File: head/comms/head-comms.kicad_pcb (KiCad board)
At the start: 2 copper layers, 30 x 20 mm, 40 parts, among them J1 conn_head_main, J3 USB_C_Receptacle_USB2.0_16P, J4 conn_chest, U1 LM66200, U2 SP48xE, U3 USBLC6-2SC6, U4 RP509x, U5 RTL8189FTV-VC-CG, Y3 26M

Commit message: finishing touches
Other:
- board text added: "GRG4UQ"
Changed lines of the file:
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@@
 		(rev "1")
 		(company "team noon")
-		(comment 1 "NanoID: rI02tsXA")
+		(comment 1 "NanoID: GRG4UQ")
 		(comment 3 "github.com/team-noon/hw1")
 		(comment 4 "Drawn By: Sam")
@@
 			(outputformat 1)
 			(mirror no)
-			(drillshape 1)
+			(drillshape 0)
 			(scaleselection 1)
-			(outputdirectory "")
+			(outputdirectory "export/")
 		)
 	)
@@
 		(layer "Edge.Cuts")
 	)
+	(gr_text "GRG4UQ"
+		(at 65 52.45 0)
+		(layer "F.SilkS")
+		(effects
+			(font
+				(size 1.5 1.5)
+				(thickness 0.3)
+				(bold yes)
+			)
+		)
+	)
 	(segment
 		(start 67.840001 66.872498)
@@
 	)
 	(segment
+		(start 71.990001 61.75)
+		(end 71.3 61.75)
+		(width 0.2)
+		(layer "F.Cu")
+		(net "Net-(J3-CC2)")
+	)
+	(via
+		(at 71.3 61.75)
+		(size 0.5)
+		(drill 0.3)
+		(layers "F.Cu" "B.Cu")
+		(net "Net-(J3-CC2)")
+	)
+	(segment
+		(start 71.3 61.75)
+		(end 72.305 61.75)
+		(width 0.2)
+		(layer "B.Cu")
+		(net "Net-(J3-CC2)")
+	)
+	(segment
 		(start 59.6 61.28)
 		(end 59.6 61.75)
@@
 	)
 	(segment
+		(start 71.99 58.75)
+		(end 71.3 58.75)
+		(width 0.2)
+		(layer "F.Cu")
+		(net "Net-(J3-CC1)")
+	)
+	(via
+		(at 71.3 58.75)
+		(size 0.5)
+		(drill 0.3)
+		(layers "F.Cu" "B.Cu")
+		(net "Net-(J3-CC1)")
+	)
+	(segment
+		(start 71.3 58.75)
+		(end 72.305 58.75)
+		(width 0.2)
+		(layer "B.Cu")
+		(net "Net-(J3-CC1)")
+	)
+	(segment
 		(start 58.5 57.485)
 		(end 58.5 58.5375)
@@
 	)
 	(segment
+		(start 72.305 60.75)
+		(end 70.924129 60.75)
+		(width 0.2)
+		(layer "B.Cu")
+		(net "Net-(J3-D+-PadA6)")
+	)
+	(segment
+		(start 70.924129 60.75)
+		(end 70.549129 61.125)
+		(width 0.2)
+		(layer "B.Cu")
+		(net "Net-(J3-D+-PadA6)")
+	)
+	(segment
+		(start 70.549129 61.125)
+		(end 69.00087 61.125)
+		(width 0.2)
+		(layer "B.Cu")
+		(net "Net-(J3-D+-PadA6)")
+	)
+	(segment
+		(start 73.05 60.75)
+		(end 72.305 60.75)
+		(width 0.2)
+		(layer "B.Cu")
+		(net "Net-(J3-D+-PadA6)")
+	)
+	(segment
+		(start 72.305 59.75)
+		(end 73.08 59.75)
+		(width 0.2)
+		(layer "B.Cu")
+		(net "Net-(J3-D+-PadA6)")
+	)
+	(segment
+		(start 68.350001 60.474131)
+		(end 68.350001 60.2625)
+		(width 0.2)
+		(layer "B.Cu")
+		(net "Net-(J3-D+-PadA6)")
+	)
+	(segment
+		(start 73.23 59.9)
+		(end 73.23 60.57)
+		(width 0.2)
+		(layer "B.Cu")
+		(net "Net-(J3-D+-PadA6)")
+	)
+	(segment
+		(start 69.00087 61.125)
+		(end 68.350001 60.474131)
+		(width 0.2)
+		(layer "B.Cu")
+		(net "Net-(J3-D+-PadA6)")
+	)
+	(segment
+		(start 73.23 60.57)
+		(end 73.05 60.75)
+		(width 0.2)
+		(layer "B.Cu")
+		(net "Net-(J3-D+-PadA6)")
+	)
+	(segment
+		(start 73.08 59.75)
+		(end 73.23 59.9)
+		(width 0.2)
+		(layer "B.Cu")
+		(net "Net-(J3-D+-PadA6)")
+	)
+	(segment
 		(start 69.3 60.2625)
 		(end 69.3 59.600001)
@@
 	)
 	(segment
+		(start 71.53 59.25)
+		(end 72.305 59.25)
+		(width 0.2)
+		(layer "B.Cu")
+		(net "Net-(J3-D--PadA7)")
+	)
+	(segment
+		(start 71.53 60.25)
+		(end 71.38 60.1)
+		(width 0.2)
+		(layer "B.Cu")
+		(net "Net-(J3-D--PadA7)")
+	)
+	(segment
+		(start 70.262499 60.25)
+		(end 70.249999 60.2625)
+		(width 0.2)
+		(layer "B.Cu")
+		(net "Net-(J3-D--PadA7)")
+	)
+	(segment
+		(start 72.305 60.25)
+		(end 71.53 60.25)
+		(width 0.2)
+		(layer "B.Cu")
+		(net "Net-(J3-D--PadA7)")
+	)
+	(segment
+		(start 71.38 60.1)
+		(end 71.38 59.4)
+		(width 0.2)
+		(layer "B.Cu")
+		(net "Net-(J3-D--PadA7)")
+	)
+	(segment
+		(start 72.305 60.25)
+		(end 70.262499 60.25)
+		(width 0.2)
+		(layer "B.Cu")
+		(net "Net-(J3-D--PadA7)")
+	)
+	(segment
+		(start 71.38 59.4)
+		(end 71.53 59.25)
+		(width 0.2)
+		(layer "B.Cu")
+		(net "Net-(J3-D--PadA7)")
+	)
+	(segment
 		(start 65.900001 63)
 		(end 65.8 63.100001)
@@
 		(net "/WiFi/XO")
 	)
-	(segment
-		(start 71.53 59.25)
-		(end 72.305 59.25)
-		(width 0.2)
-		(layer "B.Cu")
-		(net "Net-(J3-D--PadA7)")
-	)
-	(segment
-		(start 71.53 60.25)
-		(end 71.38 60.1)
-		(width 0.2)
-		(layer "B.Cu")
-		(net "Net-(J3-D--PadA7)")
-	)
-	(segment
-		(start 70.262499 60.25)
-		(end 70.249999 60.2625)
-		(width 0.2)
-		(layer "B.Cu")
-		(net "Net-(J3-D--PadA7)")
-	)
-	(segment
-		(start 72.305 60.25)
-		(end 71.53 60.25)
-		(width 0.2)
-		(layer "B.Cu")
-		(net "Net-(J3-D--PadA7)")
-	)
-	(segment
-		(start 71.38 60.1)
-		(end 71.38 59.4)
-		(width 0.2)
-		(layer "B.Cu")
-		(net "Net-(J3-D--PadA7)")
-	)
-	(segment
-		(start 72.305 60.25)
-		(end 70.262499 60.25)
-		(width 0.2)
-		(layer "B.Cu")
-		(net "Net-(J3-D--PadA7)")
-	)
-	(segment
-		(start 71.38 59.4)
-		(end 71.53 59.25)
-		(width 0.2)
-		(layer "B.Cu")
-		(net "Net-(J3-D--PadA7)")
-	)
-	(segment
-		(start 71.99 58.75)
-		(end 71.3 58.75)
-		(width 0.2)
-		(layer "F.Cu")
-		(net "Net-(J3-CC1)")
-	)
-	(via
-		(at 71.3 58.75)
-		(size 0.5)
-		(drill 0.3)
-		(layers "F.Cu" "B.Cu")
-		(net "Net-(J3-CC1)")
-	)
-	(segment
-		(start 71.3 58.75)
-		(end 72.305 58.75)
-		(width 0.2)
-		(layer "B.Cu")
-		(net "Net-(J3-CC1)")
-	)
-	(segment
-		(start 72.305 60.75)
-		(end 70.924129 60.75)
-		(width 0.2)
-		(layer "B.Cu")
-		(net "Net-(J3-D+-PadA6)")
-	)
-	(segment
-		(start 70.924129 60.75)
-		(end 70.549129 61.125)
-		(width 0.2)
-		(layer "B.Cu")
-		(net "Net-(J3-D+-PadA6)")
-	)
-	(segment
-		(start 70.549129 61.125)
-		(end 69.00087 61.125)
-		(width 0.2)
-		(layer "B.Cu")
-		(net "Net-(J3-D+-PadA6)")
-	)
-	(segment
-		(start 73.05 60.75)
-		(end 72.305 60.75)
-		(width 0.2)
-		(layer "B.Cu")
-		(net "Net-(J3-D+-PadA6)")
-	)
-	(segment
-		(start 72.305 59.75)
-		(end 73.08 59.75)
-		(width 0.2)
-		(layer "B.Cu")
-		(net "Net-(J3-D+-PadA6)")
-	)
-	(segment
-		(start 68.350001 60.474131)
-		(end 68.350001 60.2625)
-		(width 0.2)
-		(layer "B.Cu")
-		(net "Net-(J3-D+-PadA6)")
-	)
-	(segment
-		(start 73.23 59.9)
-		(end 73.23 60.57)
-		(width 0.2)
-		(layer "B.Cu")
-		(net "Net-(J3-D+-PadA6)")
-	)
-	(segment
-		(start 69.00087 61.125)
-		(end 68.350001 60.474131)
-		(width 0.2)
-		(layer "B.Cu")
-		(net "Net-(J3-D+-PadA6)")
-	)
-	(segment
-		(start 73.23 60.57)
-		(end 73.05 60.75)
-		(width 0.2)
-		(layer "B.Cu")
-		(net "Net-(J3-D+-PadA6)")
-	)
-	(segment
-		(start 73.08 59.75)
-		(end 73.23 59.9)
-		(width 0.2)
-		(layer "B.Cu")
-		(net "Net-(J3-D+-PadA6)")
-	)
-	(segment
-		(start 71.990001 61.75)
-		(end 71.3 61.75)
-		(width 0.2)
-		(layer "F.Cu")
-		(net "Net-(J3-CC2)")
-	)
-	(via
-		(at 71.3 61.75)
-		(size 0.5)
-		(drill 0.3)
-		(layers "F.Cu" "B.Cu")
-		(net "Net-(J3-CC2)")
-	)
-	(segment
-		(start 71.3 61.75)
-		(end 72.305 61.75)
-		(width 0.2)
-		(layer "B.Cu")
-		(net "Net-(J3-CC2)")
-	)
 	(zone

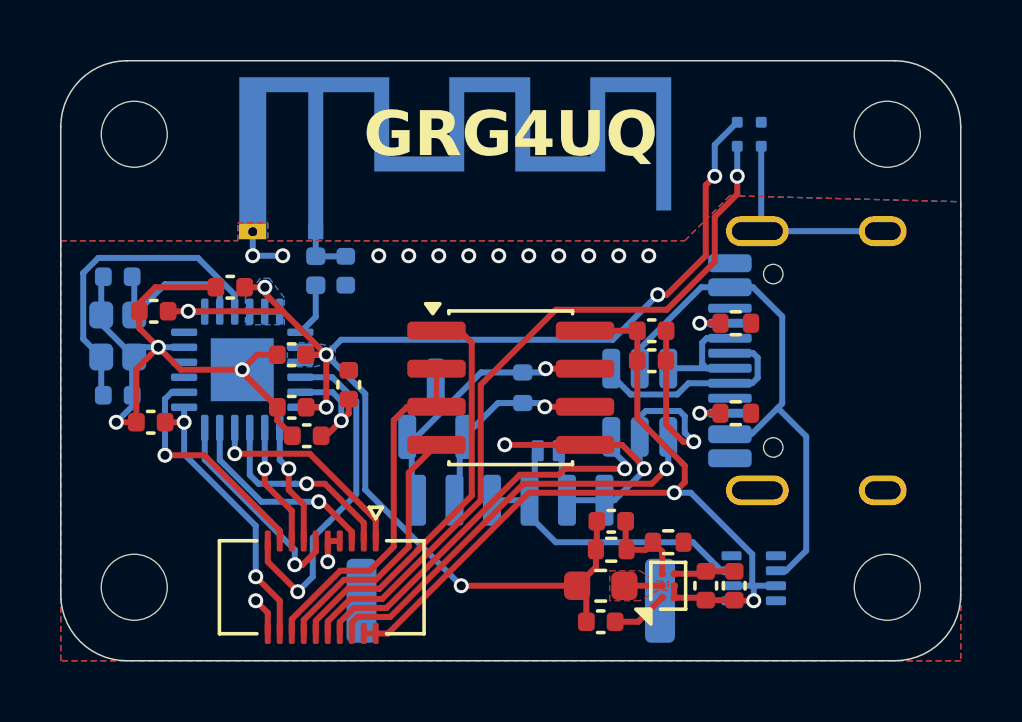
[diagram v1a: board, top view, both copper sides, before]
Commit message: fix missing ESD diode
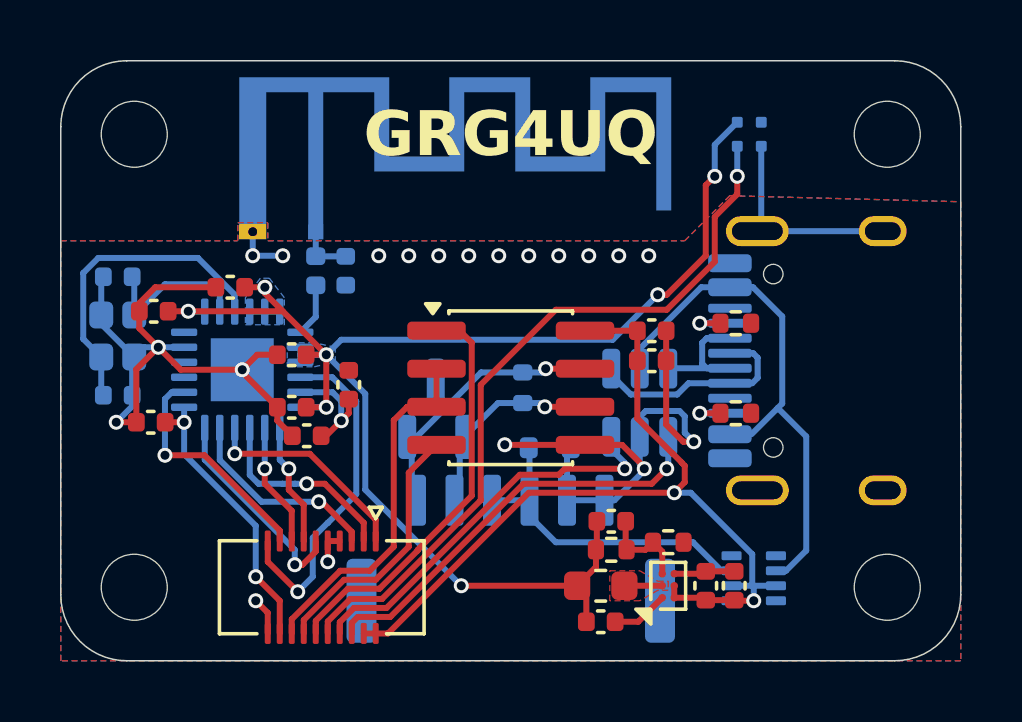
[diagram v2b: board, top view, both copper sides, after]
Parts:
- C12, C14, C15, C16, C17, C18, C2: value 0.1u -> 100n
- C57, C58: value 12p -> 10p
- D10: value ESD -> ESD5Zxx; footprint Diode_SMD:D_SOD-882 -> Diode_SMD:D_SOD-523
- moved D10 0.11 mm to (66.3, 62.9)

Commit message: larger traces, swapped connector
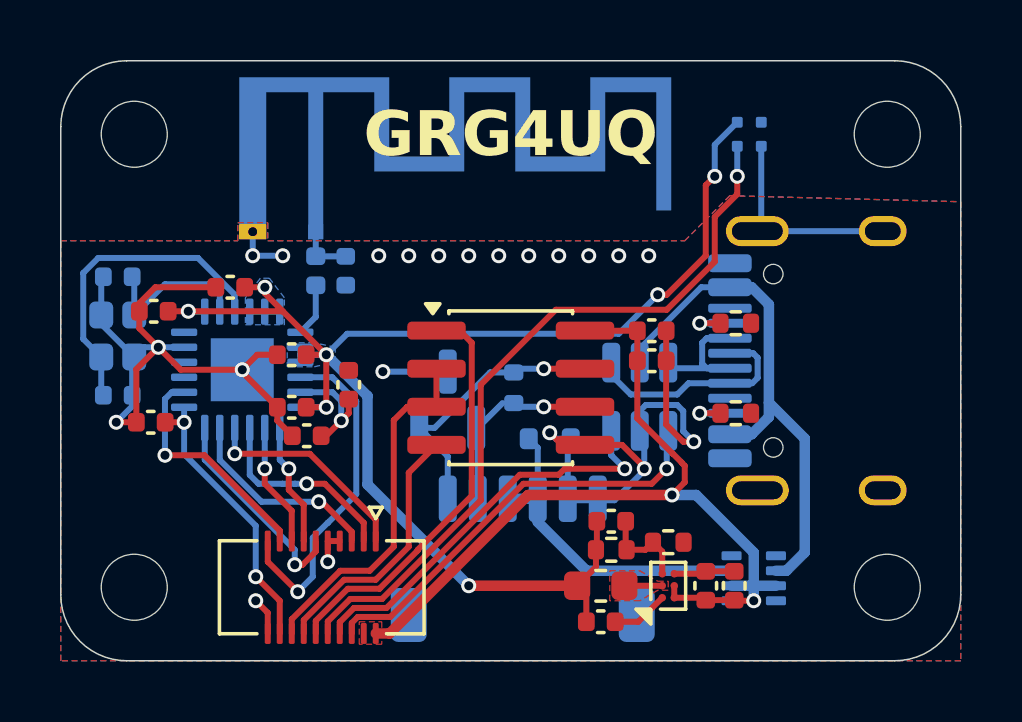
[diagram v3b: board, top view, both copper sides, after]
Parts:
- J4: footprint misc:A1257WV-S-6P-LCP -> Connector_JST:JST_SH_SM06B-SRSS-TB_1x06-1MP_P1.00mm_Horizontal
- R1: value 120 (DNF) -> 120
- moved J4 1.46 mm to (65.4, 66.6), turned to 180 degrees
- moved D1 0.50 mm to (62.9, 61.3)
- moved R1 0.30 mm to (65.1, 60.9)
- moved D10 0.30 mm to (66.3, 62.6)
- moved U3 0.20 mm to (69.3, 61.2)
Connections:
- J4 pad 1: /DB -> GND
- J4 pad 2: /DA -> GND
- J4 pad 5: GND -> /DA
- J4 pad 6: GND -> /DB
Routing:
- net GND: track 56.8 -> 59.1 mm, vias 20 -> 21
- net /DA: track 6.79 -> 5.96 mm
- net Net-(U1-VIN2): track 17.4 -> 18.0 mm
- added copper zone on F.Cu, net +5V

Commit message: move connector, cleanup traces
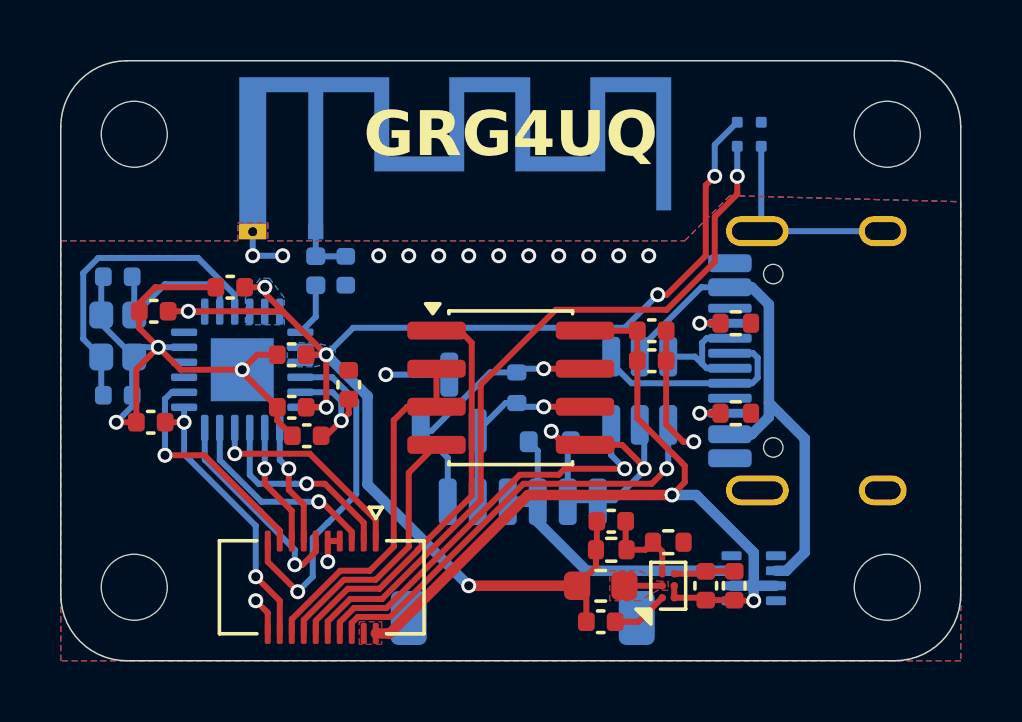
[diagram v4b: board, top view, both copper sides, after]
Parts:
- moved U3 0.20 mm to (69.3, 61.0)
- moved D1 0.11 mm to (63.0, 61.4)
- moved J4 0.10 mm to (65.4, 66.7)
- moved R1 0.10 mm to (65.2, 60.9)
- moved D10 0.10 mm to (66.3, 62.7)
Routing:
- net GND: track 59.1 -> 56.7 mm
- net Net-(J3-D--PadA7): track 4.73 -> 3.90 mm
- net Net-(U1-VIN2): track 18.0 -> 17.4 mm
